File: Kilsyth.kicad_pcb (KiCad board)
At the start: 4 copper layers, 95 x 80 mm, 153 parts, among them J1 Conn_JTAG, J2 DX07S024JJ2, J3 USB_B_Micro, J4 Conn_02x20_Counter_Clockwise, J5 Conn_02x06_Odd_Even, J6 PUSB3FR4Z, J7 PUSB3FR4Z, J8 Conn_02x06_Odd_Even, J9 Conn_02x06_Odd_Even, SW1 SW_Push, U1 DSC6001CI2A-016.0000T, U2 LFE5U-85F-6BG381C, U3 TPS65261, U4 MIC5504-1.8YM5, U5 IS25LP128F-JBLE, U6 FT600Q, U7 AS4C32M16SB, Y1 30MHz ±20ppm

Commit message: getting somewhere
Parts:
- added D10: LED, LED_SMD:LED_0603_1608Metric, F.Cu at (135.8, 57.0)
- added D3: LED, LED_SMD:LED_0603_1608Metric, F.Cu at (123.5, 57.0)
- added D4: LED, LED_SMD:LED_0603_1608Metric, F.Cu at (125.2, 57.0)
- added D5: LED, LED_SMD:LED_0603_1608Metric, F.Cu at (127.0, 57.0)
- added D6: LED, LED_SMD:LED_0603_1608Metric, F.Cu at (128.8, 57.0)
- added D7: LED, LED_SMD:LED_0603_1608Metric, F.Cu at (130.5, 57.0)
- added D8: LED, LED_SMD:LED_0603_1608Metric, F.Cu at (132.2, 57.0)
- added D9: LED, LED_SMD:LED_0603_1608Metric, F.Cu at (134.0, 57.0)
- added J10: Conn_02x01, Connector_PinHeader_2.54mm:PinHeader_2x01_P2.54mm_Vertical, F.Cu at (103.1, 56.6)
- added R15: 2K, Resistor_SMD:R_0603_1608Metric, F.Cu at (123.5, 53.5)
- added R26: 2K, Resistor_SMD:R_0603_1608Metric, F.Cu at (125.2, 53.5)
- added R30: 2K, Resistor_SMD:R_0603_1608Metric, F.Cu at (127.0, 53.5)
- added R59: 2K, Resistor_SMD:R_0603_1608Metric, F.Cu at (128.8, 53.5)
- added R60: 2K, Resistor_SMD:R_0603_1608Metric, F.Cu at (130.5, 53.5)
- added R61: 2K, Resistor_SMD:R_0603_1608Metric, F.Cu at (132.2, 53.5)
- added R62: 2K, Resistor_SMD:R_0603_1608Metric, F.Cu at (134.0, 53.5)
- added R63: 2K, Resistor_SMD:R_0603_1608Metric, F.Cu at (135.8, 53.5)
- J4: value Conn_02x20_Counter_Clockwise -> Conn_02x20_Odd_Even
- moved R19 131.9 mm to (27.0, 21.1)
- moved C7 131.9 mm to (27.1, 22.8)
- moved U4 131.9 mm to (27.1, 28.8)
- moved R20 131.3 mm to (31.0, 22.6)
- moved C6 120.5 mm to (31.0, 28.2)
- moved C48 25.6 mm to (85.4, 76.5)
- moved J9 25.3 mm to (139.0, 78.0), turned to 180 degrees
- moved J8 23.4 mm to (120.9, 56.6)
- moved U1 21.4 mm to (132.7, 114.0)
- moved J5 16.1 mm to (98.0, 56.6)
- moved J4 1.96 mm to (109.5, 64.5)
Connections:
- J4 pad 1: Net-(J4-Pad1) -> /WIDE_1
- J4 pad 10: Net-(J4-Pad10) -> /WIDE_10
- J4 pad 11: Net-(J4-Pad11) -> /WIDE_11
- J4 pad 12: Net-(J4-Pad12) -> /WIDE_12
- J4 pad 13: Net-(J4-Pad13) -> /WIDE_13
- J4 pad 14: Net-(J4-Pad14) -> /WIDE_14
- J4 pad 15: Net-(J4-Pad15) -> /WIDE_15
- J4 pad 16: Net-(J4-Pad16) -> /WIDE_16
- J4 pad 17: Net-(J4-Pad17) -> /WIDE_17
- J4 pad 18: Net-(J4-Pad18) -> /WIDE_18
- J4 pad 19: Net-(J4-Pad19) -> /WIDE_19
- J4 pad 2: Net-(J4-Pad2) -> /WIDE_2
- J4 pad 20: Net-(J4-Pad20) -> /WIDE_20
- J4 pad 21: Net-(J4-Pad21) -> /WIDE_21
- J4 pad 22: Net-(J4-Pad22) -> /WIDE_22
- J4 pad 23: Net-(J4-Pad23) -> /WIDE_23
- J4 pad 24: Net-(J4-Pad24) -> /WIDE_24
- J4 pad 25: Net-(J4-Pad25) -> /WIDE_25
- J4 pad 26: Net-(J4-Pad26) -> /WIDE_26
- J4 pad 27: Net-(J4-Pad27) -> /WIDE_27
- J4 pad 28: Net-(J4-Pad28) -> /WIDE_28
- J4 pad 29: Net-(J4-Pad29) -> /WIDE_29
- J4 pad 3: Net-(J4-Pad3) -> /WIDE_3
- J4 pad 30: Net-(J4-Pad30) -> /WIDE_30
- J4 pad 31: Net-(J4-Pad31) -> /WIDE_31
- J4 pad 32: Net-(J4-Pad32) -> /WIDE_32
- J4 pad 33: Net-(J4-Pad33) -> /WIDE_33
- J4 pad 34: Net-(J4-Pad34) -> /WIDE_34
- J4 pad 35: Net-(J4-Pad35) -> /WIDE_35
- J4 pad 36: Net-(J4-Pad36) -> /WIDE_36
- J4 pad 37: Net-(J4-Pad37) -> /WIDE_37
- J4 pad 38: Net-(J4-Pad38) -> /WIDE_38
- J4 pad 39: Net-(J4-Pad39) -> /WIDE_39
- J4 pad 4: Net-(J4-Pad4) -> /WIDE_4
- J4 pad 40: Net-(J4-Pad40) -> /WIDE_40
- J4 pad 5: Net-(J4-Pad5) -> /WIDE_5
- J4 pad 6: Net-(J4-Pad6) -> /WIDE_6
- J4 pad 7: Net-(J4-Pad7) -> /WIDE_7
- J4 pad 8: Net-(J4-Pad8) -> /WIDE_8
- J4 pad 9: Net-(J4-Pad9) -> /WIDE_9
- J5 pad 1: /PMOD0_1 -> +3V3
- J5 pad 10: GND -> /PMOD0_6
- J5 pad 11: /PMOD0_VCC -> /PMOD0_1
- J5 pad 12: /PMOD0_VCC -> /PMOD0_5
- J5 pad 2: /PMOD0_2 -> +3V3
- J5 pad 3: /PMOD0_3 -> GND
- J5 pad 4: /PMOD0_4 -> GND
- J5 pad 5: /PMOD0_5 -> /PMOD0_4
- J5 pad 6: /PMOD0_6 -> /PMOD0_8
- J5 pad 7: /PMOD0_7 -> /PMOD0_3
- J5 pad 8: /PMOD0_8 -> /PMOD0_7
- J5 pad 9: GND -> /PMOD0_2
- J8 pad 1: /PMOD1_1 -> +3V3
- J8 pad 10: GND -> /PMOD1_6
- J8 pad 11: /PMOD1_VCC -> /PMOD1_1
- J8 pad 12: /PMOD1_VCC -> /PMOD1_5
- J8 pad 2: /PMOD1_2 -> +3V3
- J8 pad 3: /PMOD1_3 -> GND
- J8 pad 4: /PMOD1_4 -> GND
- J8 pad 5: /PMOD1_5 -> /PMOD1_4
- J8 pad 6: /PMOD1_6 -> /PMOD1_8
- J8 pad 7: /PMOD1_7 -> /PMOD1_3
- J8 pad 8: /PMOD1_8 -> /PMOD1_7
- J8 pad 9: GND -> /PMOD1_2
- J9 pad 1: /PMOD2_1 -> +3V3
- J9 pad 10: GND -> /PMOD2_6
- J9 pad 11: /PMOD2_VCC -> /PMOD2_1
- J9 pad 12: /PMOD2_VCC -> /PMOD2_5
- J9 pad 2: /PMOD2_2 -> +3V3
- J9 pad 3: /PMOD2_3 -> GND
- J9 pad 4: /PMOD2_4 -> GND
- J9 pad 5: /PMOD2_5 -> /PMOD2_4
- J9 pad 6: /PMOD2_6 -> /PMOD2_8
- J9 pad 7: /PMOD2_7 -> /PMOD2_3
- J9 pad 8: /PMOD2_8 -> /PMOD2_7
- J9 pad 9: GND -> /PMOD2_2
- U2 pad A10: /BANK0 -> /WIDE_36
- U2 pad A11: /BANK0 -> /WIDE_37
- U2 pad A12: /PMOD0_5 -> /PMOD0_1
- U2 pad A13: /PMOD1_4 -> /PMOD0_3
- U2 pad A14: /PMOD0_2 -> /PMOD1_1
- U2 pad A16: /PMOD2_5 -> /PMOD1_7
- U2 pad A17: /PMOD2_2 -> /PMOD2_1
- U2 pad A18: /PMOD2_1 -> /PMOD2_6
- U2 pad A19: /PMOD2_8 -> /PMOD2_7
- U2 pad A2: /BANK7 -> /WIDE_7
- U2 pad A3: /BANK7 -> /WIDE_11
- U2 pad A4: /BANK7 -> /WIDE_15
- U2 pad A5: /BANK7 -> /WIDE_19
- U2 pad A6: /BANK0 -> /WIDE_23
- U2 pad A7: /BANK0 -> /WIDE_28
- U2 pad A8: /BANK0 -> /WIDE_30
- U2 pad A9: /BANK0 -> /WIDE_31
- U2 pad B1: /BANK7 -> /WIDE_8
- U2 pad B10: /BANK0 -> /WIDE_35
- U2 pad B11: /BANK0 -> /WIDE_39
- U2 pad B12: /PMOD0_7 -> /PMOD0_5
- U2 pad B13: /PMOD0_4 -> /PMOD0_7
- U2 pad B15: /PMOD0_8 -> /PMOD1_2
- U2 pad B16: Net-(U2-PadB16) -> /PMOD1_4
- U2 pad B17: /PMOD2_3 -> /PMOD2_5
- U2 pad B18: Net-(U2-PadB18) -> /PMOD2_3
- U2 pad B19: Net-(U2-PadB19) -> /PMOD2_8
- U2 pad B2: /BANK7 -> /WIDE_10
- U2 pad B20: Net-(U2-PadB20) -> /PMOD2_4
- U2 pad B3: /BANK7 -> /WIDE_14
- U2 pad B4: /BANK7 -> /WIDE_18
- U2 pad B5: /BANK7 -> /WIDE_22
- U2 pad B6: /BANK0 -> /WIDE_26
- U2 pad B8: /BANK0 -> /WIDE_29
- U2 pad B9: /BANK0 -> /WIDE_34
- U2 pad C1: /BANK7 -> /WIDE_5
- U2 pad C10: /BANK0 -> /WIDE_38
- U2 pad C11: /BANK0 -> /WIDE_40
- U2 pad C12: /PMOD1_6 -> /PMOD0_6
- U2 pad C13: /PMOD1_3 -> /PMOD0_8
- U2 pad C14: /PMOD1_1 -> /PMOD1_5
- U2 pad C15: /PMOD2_7 -> /PMOD1_3
- U2 pad C16: /PMOD2_4 -> /PMOD1_8
- U2 pad C17: Net-(U2-PadC17) -> /PMOD2_2
- U2 pad C2: /BANK7 -> /WIDE_9
- U2 pad C3: /BANK7 -> /WIDE_13
- U2 pad C4: /BANK7 -> /WIDE_17
- U2 pad C5: /BANK7 -> /WIDE_21
- U2 pad C6: /BANK0 -> /WIDE_25
- U2 pad C7: /BANK0 -> /WIDE_27
- U2 pad C8: /BANK0 -> /WIDE_32
- U2 pad C9: /BANK0 -> /WIDE_33
- U2 pad D1: /BANK7 -> /WIDE_6
- U2 pad D10: /BANK0 -> Net-(U2-PadD10)
- U2 pad D11: CLK_16MHz -> Net-(U2-PadD11)
- U2 pad D12: /PMOD0_6 -> /PMOD0_2
- U2 pad D13: /PMOD0_3 -> /PMOD0_4
- U2 pad D14: /PMOD0_1 -> Net-(U2-PadD14)
- U2 pad D15: /PMOD2_6 -> /PMOD1_6
- U2 pad D2: /BANK7 -> /WIDE_12
- U2 pad D3: /BANK7 -> /WIDE_16
- U2 pad D5: /BANK7 -> /WIDE_24
- U2 pad D6: /BANK0 -> Net-(U2-PadD6)
- U2 pad D7: /BANK0 -> Net-(U2-PadD7)
- U2 pad D8: /BANK0 -> Net-(U2-PadD8)
- U2 pad D9: /BANK0 -> Net-(U2-PadD9)
- U2 pad E1: /BANK7 -> /WIDE_4
- U2 pad E10: /BANK0 -> Net-(U2-PadE10)
- U2 pad E11: /PMOD1_7 -> Net-(U2-PadE11)
- U2 pad E12: /PMOD1_5 -> Net-(U2-PadE12)
- U2 pad E13: /PMOD1_2 -> Net-(U2-PadE13)
- U2 pad E14: /PMOD1_8 -> Net-(U2-PadE14)
- U2 pad E2: /BANK7 -> /WIDE_3
- U2 pad E3: /BANK7 -> Net-(U2-PadE3)
- U2 pad E4: /BANK7 -> /WIDE_20
- U2 pad E5: /BANK7 -> Net-(U2-PadE5)
- U2 pad E6: /BANK0 -> Net-(U2-PadE6)
- U2 pad E7: /BANK0 -> Net-(U2-PadE7)
- U2 pad E8: /BANK0 -> Net-(U2-PadE8)
- U2 pad E9: /BANK0 -> Net-(U2-PadE9)
- U2 pad F2: /BANK7 -> /WIDE_2
- U2 pad F3: /BANK7 -> /WIDE_1
- U2 pad F4: /BANK7 -> Net-(U2-PadF4)
- U2 pad F5: /BANK7 -> Net-(U2-PadF5)
- U2 pad G3: /BANK7 -> CLK_16MHz
- U2 pad G5: /BANK7 -> Net-(U2-PadG5)
- U2 pad H3: /BANK7 -> Net-(U2-PadH3)
- U2 pad H4: /BANK7 -> Net-(U2-PadH4)
- U2 pad H5: /BANK7 -> Net-(U2-PadH5)
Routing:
- net /WIDE_40: track 0.00 -> 54.4 mm, vias 0 -> 2
- net /WIDE_38: track 0.00 -> 53.1 mm, vias 0 -> 2
- net /WIDE_39: track 0.00 -> 52.2 mm, vias 0 -> 2
- net /WIDE_35: track 0.00 -> 51.5 mm, vias 0 -> 2
- net /WIDE_33: track 0.00 -> 51.2 mm, vias 0 -> 4
- net /WIDE_37: track 0.00 -> 50.8 mm, vias 0 -> 2
- net /WIDE_36: track 0.00 -> 50.0 mm
- net /WIDE_34: track 0.00 -> 49.8 mm
- net /PMOD2_5: track 0.00 -> 43.2 mm
- net /WIDE_32: track 0.00 -> 42.7 mm, vias 0 -> 2
- net /PMOD2_1: track 0.00 -> 40.1 mm
- net /PMOD2_2: track 0.00 -> 39.9 mm, vias 0 -> 1
- net /PMOD2_6: track 0.00 -> 39.7 mm
- net /WIDE_30: track 0.00 -> 39.6 mm
- net /PMOD0_5: track 0.00 -> 37.9 mm, vias 0 -> 1
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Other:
- board text added: "GND"

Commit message: Final RevA
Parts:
- removed C7: 22u, Capacitor_SMD:C_0603_1608Metric
- removed R19: 0R, Resistor_SMD:R_0603_1608Metric
- removed TP4: TestPoint, TestPoint:TestPoint_Pad_D1.0mm
- removed U4: MIC5504-1.8YM5, Package_TO_SOT_SMD:SOT-23-5
- added G***: LOGO, xil:logo_23x19mm, F.Cu at (123.8, 113.4)
- added G***: LOGO, xil:oshw_logo, F.Cu at (139.0, 109.2)
- added J11: Conn_02x04_Odd_Even, Connector_PinHeader_2.54mm:PinHeader_2x04_P2.54mm_Vertical_SMD, F.Cu at (58.6, 112.8)
- C38, C39, C40, C44, C45, C46, C47, C48, C49, C50, C51, C52, C53, C54, C56, C58, C59, C60, C61, C62, C64, C65: moved to B.Cu
- C6: value 10u -> 100n; moved to B.Cu
- moved C36 148.8 mm to (132.6, 80.2), turned to 90 degrees
- moved C35 135.2 mm to (131.0, 80.2), turned to 90 degrees
- moved C41 129.9 mm to (127.0, 100.2), turned to 270 degrees
- moved C43 119.4 mm to (141.4, 100.2), turned to 270 degrees
- moved C32 114.5 mm to (129.4, 80.2), turned to 90 degrees
- moved C42 112.1 mm to (131.0, 100.2), turned to 270 degrees
- moved C56 109.3 mm to (104.5, 87.8)
- moved C61 106.3 mm to (103.2, 104.2), turned to 90 degrees
- moved C67 105.2 mm to (104.8, 101.0), turned to 270 degrees
- moved C64 102.9 mm to (108.0, 104.2), turned to 90 degrees
- moved C6 101.0 mm to (108.6, 92.8)
- moved R20 100.6 mm to (88.2, 105.4)
- moved C63 100.3 mm to (103.2, 101.0), turned to 270 degrees
- moved C65 98.7 mm to (106.4, 104.2), turned to 90 degrees
- moved C66 98.0 mm to (108.0, 101.0), turned to 270 degrees
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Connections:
- C6 pad 1: +5V -> +2V5
- U2 pad G5: Net-(U2-PadG5) -> FT_GPIO1
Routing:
- net +3V3: track 52.9 -> 117.0 mm, vias 46 -> 54
- net GND: track 173.7 -> 223.0 mm, vias 155 -> 149
- net FT_GPIO0: track 11.4 -> 37.9 mm, vias 0 -> 2
- net /FLASH_CSn: track 42.0 -> 61.3 mm
- net /FLASH_MISO: track 40.7 -> 58.9 mm, vias 0 -> 2
- net /FLASH_WPn: track 37.2 -> 55.1 mm, vias 0 -> 2
- net /FLASH_HOLDn: track 36.5 -> 53.9 mm
- net FT_GPIO1: track 0.00 -> 16.4 mm, vias 0 -> 2
- net /FLASH_SCK: track 41.4 -> 51.3 mm, vias 2 -> 3
- net /FLASH_MOSI: track 40.7 -> 48.1 mm, vias 2 -> 3
- net CLK_16MHz: track 13.9 -> 20.3 mm
- net DONE: track 30.1 -> 23.8 mm, vias 0 -> 2
- net Net-(R24-Pad1): track 21.3 -> 27.5 mm, vias 0 -> 2
- net Net-(R1-Pad2): track 25.5 -> 21.4 mm
- net /JTAG_TCK: track 28.3 -> 32.2 mm, vias 3 -> 2
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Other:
- board text added: "+"
- board text added: "-"
- board text added: "1"
- board text added: "2"
- board text added: "3"
- board text added: "39"
- board text added: "4"
- board text added: "40"
- board text added: "5"
- board text added: "6"
- board text added: "7"
- board text added: "8"
- board text added: "@kbeckmann 2018"
- board text added: "DONE"
- board text added: "KILSYTH RevA"
- board text added: "PMOD0"
- board text added: "PMOD1"
- board text added: "PMOD2"
- board text added: "TCK"
- board text added: "TDI"
- board text added: "TDO"
- board text added: "TMS"
- board text added: "~PROGRAM~"

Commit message: Final touches
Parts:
- moved C45 0.38 mm to (108.8, 91.3)
- moved C6 0.25 mm to (108.8, 92.8)
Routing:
- net +2V5: track 27.8 -> 27.2 mm

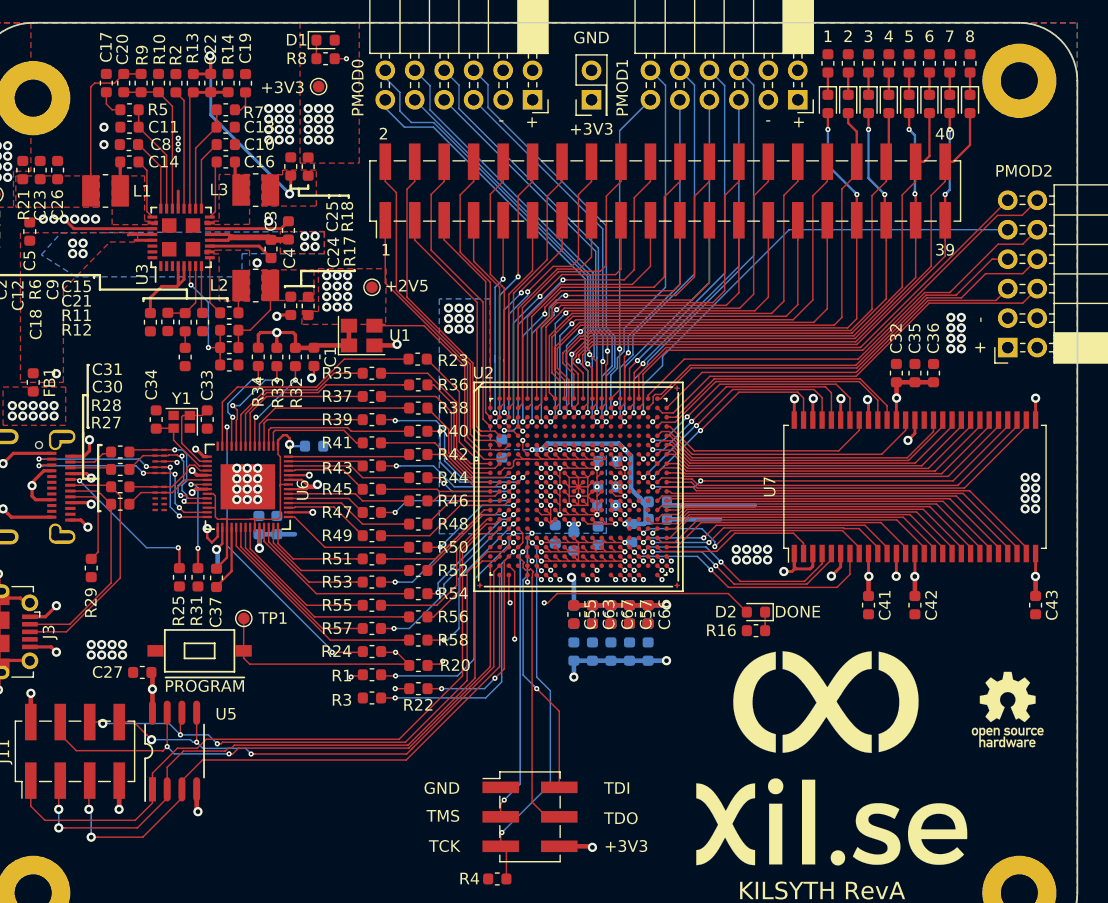
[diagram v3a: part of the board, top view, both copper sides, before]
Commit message: Changed from 4 to 5 mil spacing.. HELL.
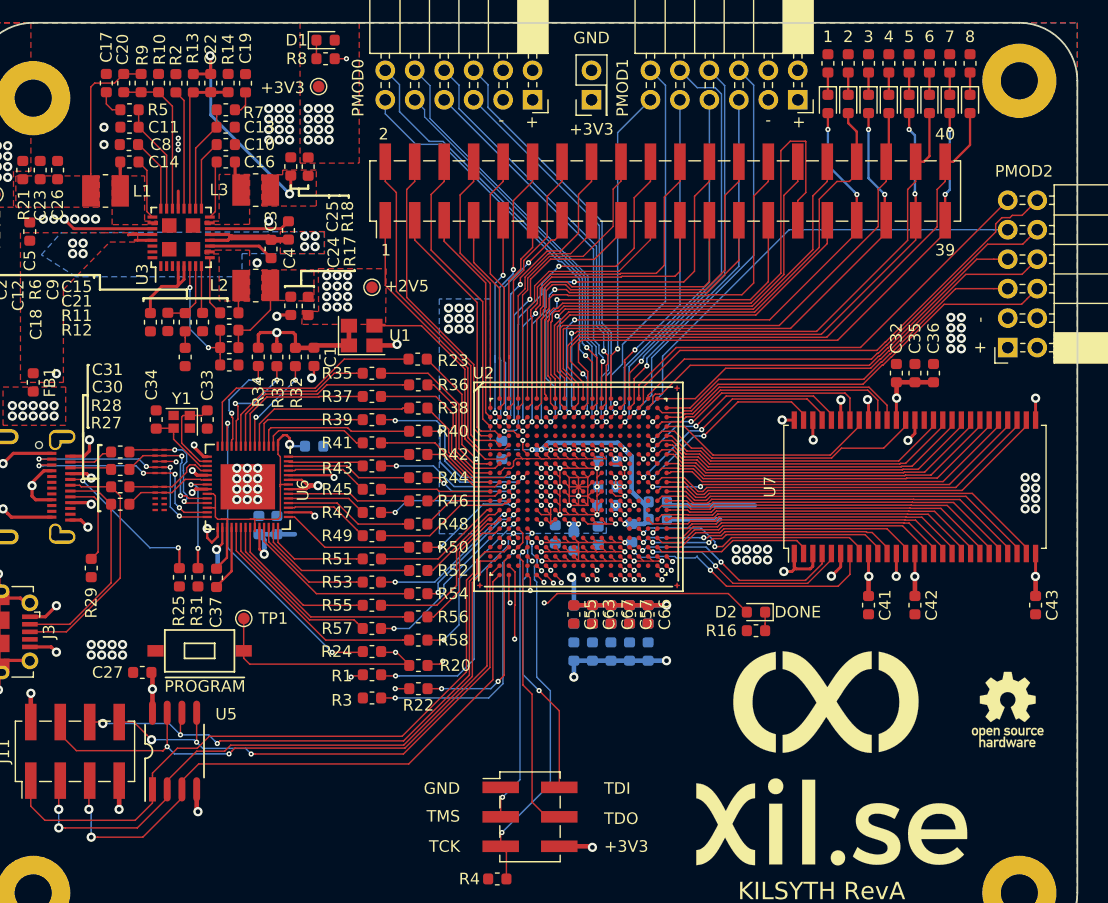
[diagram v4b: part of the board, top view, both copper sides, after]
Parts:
- moved C52 0.13 mm to (95.4, 86.8)
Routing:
- net /WIDE_29: track 36.1 -> 50.0 mm
- net +3V3: track 117.0 -> 121.7 mm
- net /WIDE_33: track 51.2 -> 47.7 mm
- net /WIDE_34: track 49.8 -> 46.9 mm
- net GND: track 223.4 -> 226.2 mm, vias 149 -> 147
- net /WIDE_31: track 37.3 -> 34.7 mm
- net /PMOD1_6: track 34.2 -> 36.7 mm
- net /WIDE_36: track 50.0 -> 47.8 mm
- net /WIDE_35: track 51.5 -> 49.7 mm
- net /RAM_DQ13: track 20.8 -> 19.0 mm
- net /RAM_DQ14: track 21.3 -> 19.8 mm
- net /RAM_DQ15: track 18.7 -> 17.2 mm
- net /WIDE_23: track 28.4 -> 29.9 mm
- net /WIDE_32: track 42.7 -> 41.5 mm
- net /WIDE_27: track 35.1 -> 36.2 mm
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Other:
- net class Default: clearance 0.1016 -> 0.127
- rule trace_clearance: 0.1016 -> 0.127

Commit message: Last minute changes
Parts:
- added J12: Conn_02x04_Odd_Even, Connector_PinHeader_2.54mm:PinHeader_2x04_P2.54mm_Vertical_SMD, F.Cu at (76.8, 122.3)
- moved G*** 1.02 mm to (138.0, 109.0)
- moved G*** 0.46 mm to (123.5, 113.8)
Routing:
- net +3V3: track 121.7 -> 135.3 mm, vias 54 -> 59
